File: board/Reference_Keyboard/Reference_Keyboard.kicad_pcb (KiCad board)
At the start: 2 copper layers, 176 x 105 mm, 90 parts, among them J1 Conn_01x03_Pin, J2 USB_C_Receptacle_USB2.0, J4 84953-4, SW1 SW_Push, SW10 SW_Push, SW11 SW_Push, SW12 SW_Push, SW13 SW_Push, SW14 SW_Push, SW15 SW_Push, SW16 SW_Push, SW17 SW_Push, SW18 SW_Push, SW19 SW_Push, SW2 SW_Push, SW20 SW_Push, SW21 SW_Push, SW22 SW_Push, SW23 SW_Push, SW24 SW_Push, SW25 SKQGAFE010, SW26 RotaryEncoder_Switch, SW27 SKQGAFE010, SW28 SKQGAFE010, SW3 SW_Push, SW4 SW_Push, SW5 SW_Push, SW6 SW_Push, SW7 SW_Push, SW8 SW_Push, SW9 SW_Push, U1 RP2040, U2 W25Q16JVSSIM, U3 LM1117RS-3.3, Y1 NX3225SA-12MHz-STD-CSR-6

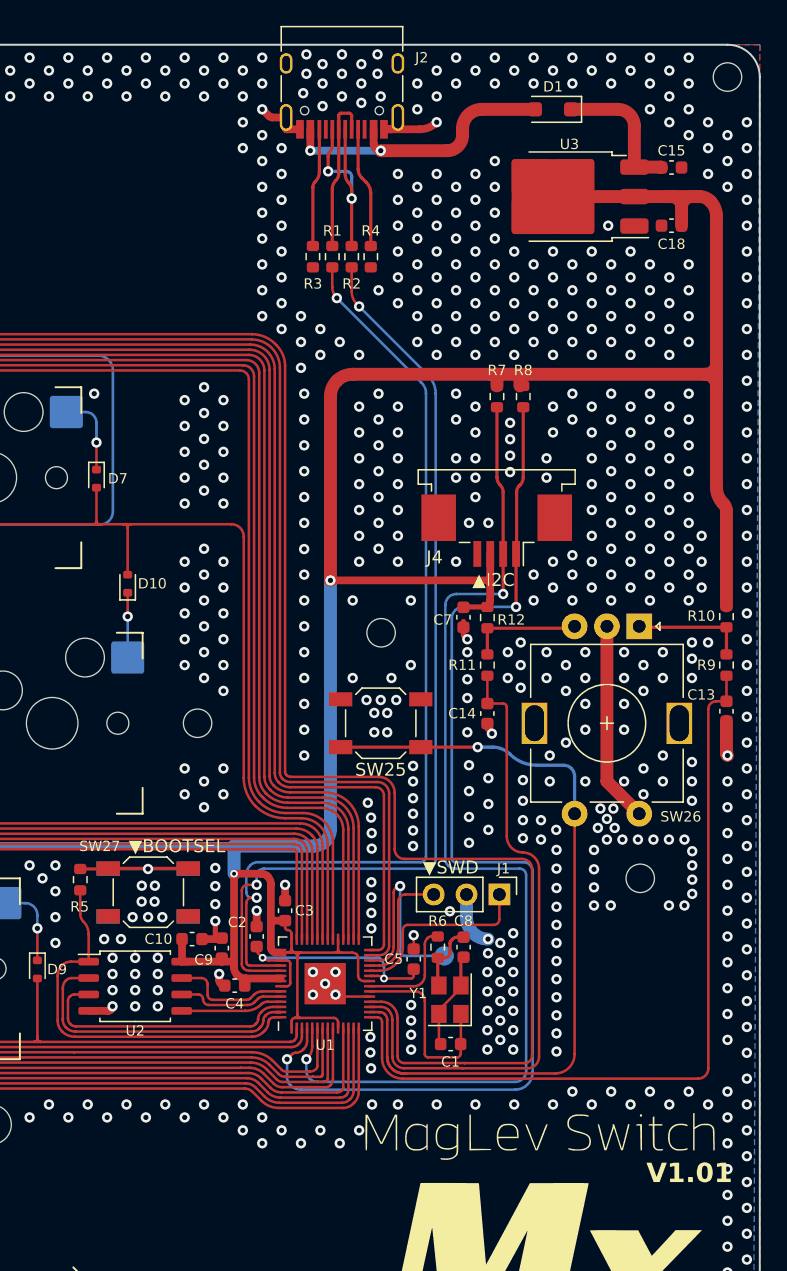
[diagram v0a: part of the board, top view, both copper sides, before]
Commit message: Add a current protection circuit
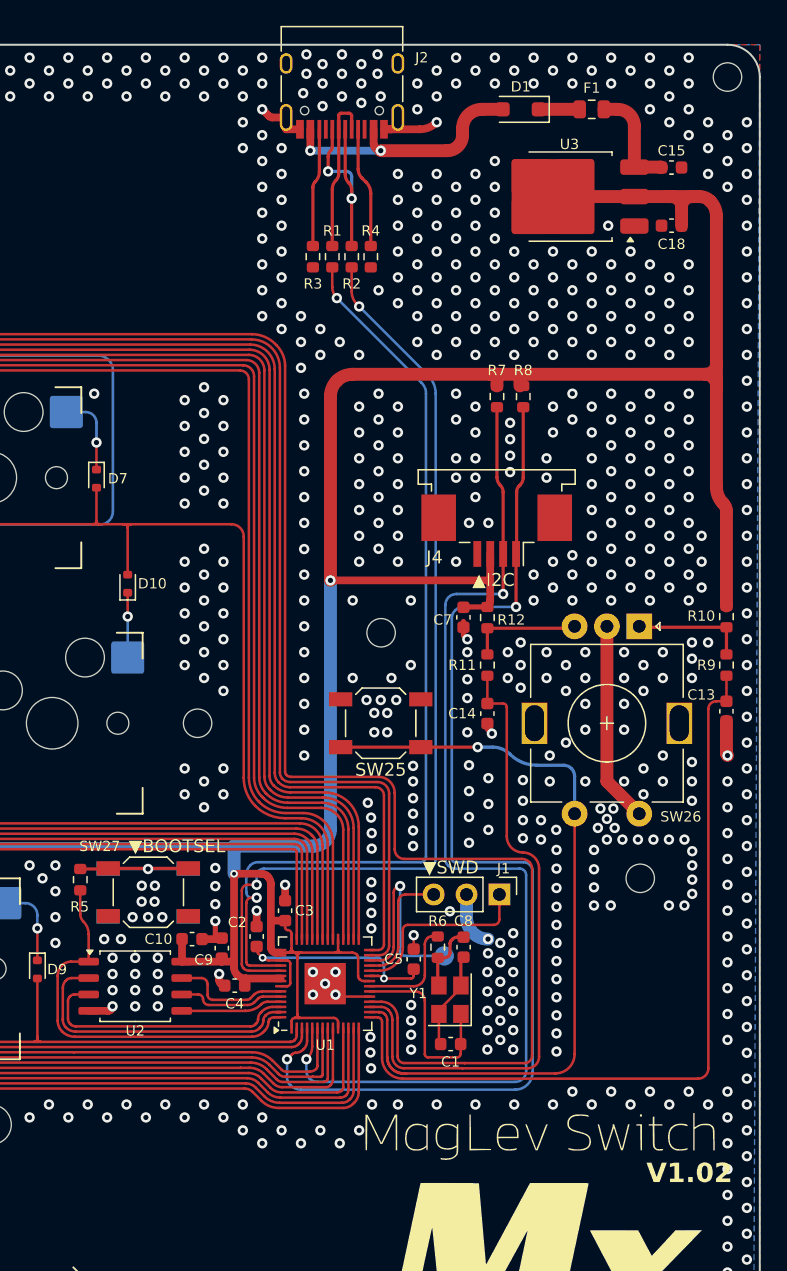
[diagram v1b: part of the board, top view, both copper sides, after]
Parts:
- added F1: Polyfuse, Fuse:Fuse_0805_2012Metric, F.Cu at (240.0, 55.5)
- D1: value RB161MM-20TR -> RB161MM-20TR
- moved D1 2.50 mm to (234.5, 55.5)
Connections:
- D1 pad 1: +5V -> Net-(D1-K)
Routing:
- net Net-(D1-K): track 0.00 -> 3.16 mm
- net +5V: track 10.9 -> 8.33 mm
- net Net-(D1-A): track 22.9 -> 20.4 mm
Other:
- board text added: "V1.02"
- board text removed: "V1.01"
